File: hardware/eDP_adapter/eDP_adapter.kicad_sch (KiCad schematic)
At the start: 85 parts, among them J1 DF12NB(3.0)-30DS-0.5V(51), J2 DF12NB(3.0)-30DS-0.5V(51), J3 Conn_01x40, J4 Barrel_Jack_MountingPin, Q1 NX3008NBKW,115, U1 NCS8801, U2 TLV62569APDRL, U3 MT3608, U5 TPNCP115ASN120T2G, X1 24MHz, CL=18PF

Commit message: Add I2C connector for touch and replace 40pin touch with 30pin. Separate schematics in sheets. Impedance control on diff pairs
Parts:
- removed C10, C13, C18, C21, C26, C3, C5, C7: 0.1uF, Library:C_0402_1005Metric, symbol Periph-altium-import:0_CAP
- removed C11, C20, C22, C25, C4, C8, C9: 2.2uF, Library:C_0402_1005Metric, symbol Periph-altium-import:0_CAP
- removed C12, C2, C24: 10uF 25V, Capacitor_SMD:C_0805_2012Metric, symbol Periph-altium-import:0_CAP
- removed C6: 100pF, Capacitor_SMD:C_0201_0603Metric, symbol Device:C
- removed D2: 1N5819WS, Diode_SMD:D_SOD-323, symbol Diode:1N5819WS
- removed FB4, FB5, FB6, FB7, FB8, FB9: CBG160808U601T, Inductor_SMD:L_0603_1608Metric, symbol Device:FerriteBead_Small
- removed J1, J2: DF12NB(3.0)-30DS-0.5V(51), Library:DF12NB3030DP05V51, symbol DF12NB_3.0_-30DP-0.5V_51_:DF12NB_3.0_-30DP-0.5V_51_
- removed J3: Conn_01x40, Library:FPC-SMD_40P-P0.50_L4.4-W25.6, symbol Connector_Generic:Conn_01x40
- removed J4: Barrel_Jack_MountingPin, Library:DC-IN-SMD_DC-045A-13A, symbol Connector:Barrel_Jack_Switch_MountingPin
- removed JP1, JP2: SolderJumper_2_Open, Jumper:SolderJumper-2_P1.3mm_Open_RoundedPad1.0x1.5mm, symbol Jumper:SolderJumper_2_Open
- removed JP3: SolderJumper_3_Bridged12, Jumper:SolderJumper-3_P1.3mm_Bridged12_RoundedPad1.0x1.5mm, symbol Jumper:SolderJumper_3_Bridged12
- removed L1: 22uH, Inductor_SMD:L_Cenker_CKCS4020, symbol CKCS201610-2.2UH/M-N_1
- removed L2: 2.2uH, Library:Murata_DFE201612P-2R2M=P2, symbol Periph-altium-import:0_L
- removed Q1: NX3008NBKW,115, Package_TO_SOT_SMD:SOT-323_SC-70, symbol Transistor_FET:2N7002
- removed R10, R13: 0, Resistor_SMD:R_0402_1005Metric, symbol Device:R
- removed R11: 15k, Resistor_SMD:R_0201_0603Metric, symbol Device:R
- removed R12: 4.7k, Resistor_SMD:R_0201_0603Metric, symbol Device:R
- removed R14: 100k, Resistor_SMD:R_0402_1005Metric, symbol Device:R
- removed R15, R19: 10k, Resistor_SMD:R_0402_1005Metric, symbol Device:R
- removed R20: 150K 1%, Resistor_SMD:R_0402_1005Metric, symbol R_0402_EU
- removed R21: 8.06K 1%, Resistor_SMD:R_0402_1005Metric, symbol R_0402_EU_1
- removed R9: 10K, Resistor_SMD:R_0402_1005Metric, symbol Device:R
- removed TP1, TP12, TP13, TP14, TP15, TP16, TP2, TP3, TP4, TP5, TP6, TP7, TP8, TP9: TestPoint_Small, TestPoint:TestPoint_Pad_D1.0mm, symbol Connector:TestPoint_Small
- removed U2: TLV62569APDRL, Package_TO_SOT_SMD:SOT-563, symbol Regulator_Switching:TLV62569DRL
- removed U3: MT3608, Package_TO_SOT_SMD:SOT-23-6, symbol Regulator_Switching:MT3608
- removed U5: TPNCP115ASN120T2G, Package_TO_SOT_SMD:SOT-23-5, symbol Regulator_Linear:NCP115AMX250TCG
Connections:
- net GND: now also C32.1; no longer C32.2
- net XTALI: now also C32.2; no longer C32.1
- net DPO0_P: now reaches C15.1, CR2.2, CR2.9, U1.36 (DPO0_P)
- net DPO1_P: now reaches C23.1, CR2.5, CR2.6, U1.38 (DPO1_P)
- net DPAUX_P: now reaches C17.1, CR1.4, CR1.7, U1.33 (DPAUX_P)
- net DPAUX_N: now reaches C16.1, CR1.5, CR1.6, U1.34 (DPAUX_N)
- net DPO0_N: now reaches C14.1, CR2.1, CR2.10, U1.35 (DPO0_N)
- net DPO1_N: now reaches C1.1, CR2.4, CR2.7, U1.37 (DPO1_N)
- no-connect marks 26 -> 2
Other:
- added sheet IO (eDP_adapter_IO.kicad_sch)
- added sheet POWER (eDP_adapter_power.kicad_sch)
- note removed: "2.5 to 3.3V: HSVDD33 RGB mode (1.8V allowable) or LVDS XVDD33 is for XTAL DVDD33 for digital VIO controls if RGB is down to 1.8V or LVDS 2.5V"
- note removed: "LCD_D0"
- note removed: "LCD_D1"
- note removed: "LCD_D10"
- note removed: "LCD_D11"
- note removed: "LCD_D12"
- note removed: "LCD_D13"
- note removed: "LCD_D14"
- note removed: "LCD_D15"
- note removed: "LCD_D16"
- note removed: "LCD_D17"
- note removed: "LCD_D18"
- note removed: "LCD_D19"
- note removed: "LCD_D2"
- note removed: "LCD_D20"
- note removed: "LCD_D21"
- note removed: "LCD_D22"
- note removed: "LCD_D23"
- note removed: "LCD_D3"
- note removed: "LCD_D4"
- note removed: "LCD_D5"
- note removed: "LCD_D6"
- note removed: "LCD_D7"
- note removed: "LCD_D8"
- note removed: "LCD_D9"
- note removed: "NCS8801 Channel and polarity swap supported Built-in video test pattern Reset defaults (2048x1536) 0x00: default 24-bit / 4 lanes / 1.62Gbps / no hardware training 0x05: no polarity inverse 0x09: normal video 0x0C: RGB mode / NS mode 0x0D: 4-lane order no reverse 0x0F: no LVDS inverse, no ODD/EVEN swap 0x10-0x11: Htotal 2208 (0x08A0) 0x12-0x13: Hstart 10 (0x000A) 0x14-0x15: Hactive 2048 (0x0800) 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"
- note removed: "North connector"
- note removed: "RSTB is active low"
- note removed: "South connector"
- note removed: "TODO: XTAL was MISSING !!! add test points for power (better: solder jumpers to allow disconnection) add 6-pin I2C connector"
- note removed: "TP_RST is active low (GT911 IC) TP_INT is configurable (sets I2C address at startup)"
- note removed: "The IC may require a higher voltage"
- note removed: "Touch panel power: NV156FHM-T01 3.3V B156XTK01.0 5V"
- note removed: "Vth=1.1V"
- note removed: "Vth=1.2V"
- note removed: "Vth=1V"
- note removed: "about 10ms delay (>50us)"
- note removed: "skew < 100mil (LVDS) or 300mil (RGB)"
- note removed: "soldiercrab TLV62569ADRLR"
- moved on the sheet: C1, C14, C15, C16, C17, C19, C23, C32, CR1, CR2, CR3, R1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

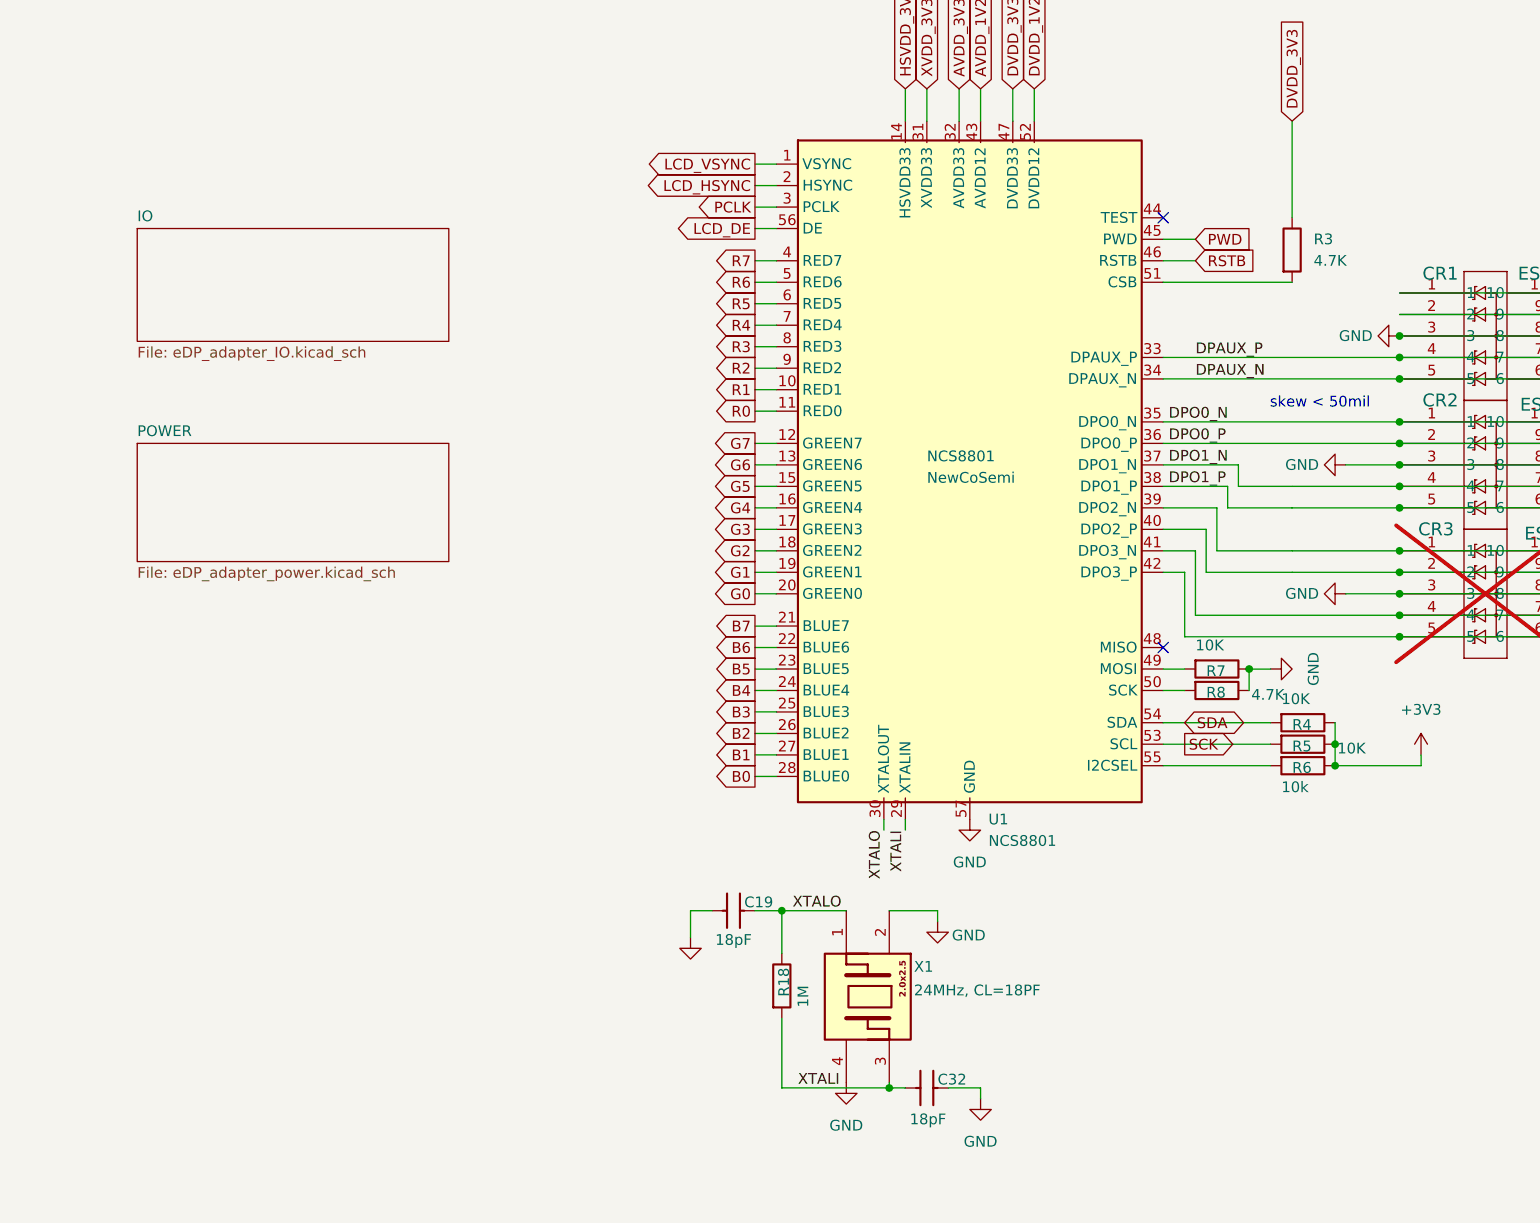
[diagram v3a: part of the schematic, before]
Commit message: change eDP adapter for dual channel LVDS input mode
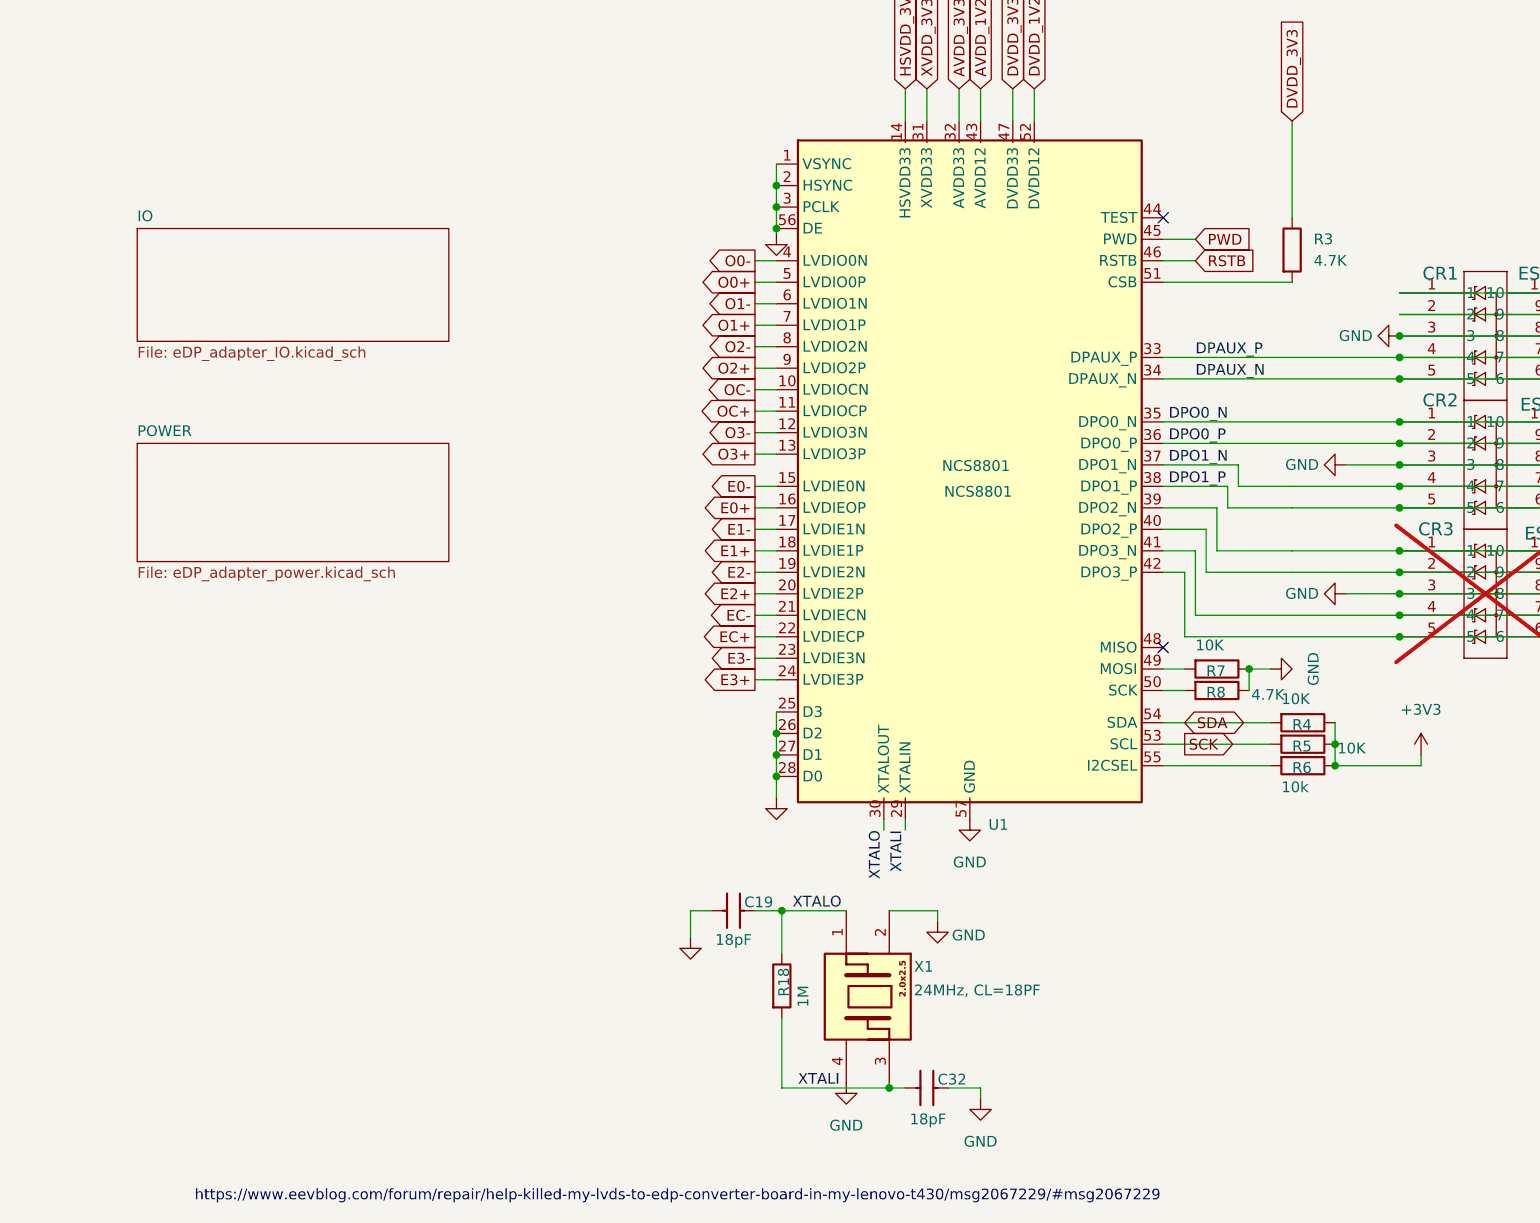
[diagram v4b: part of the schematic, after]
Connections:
- net B0 is gone; now on net GND: U1.28 (D0)
- net B1 is gone; now on net GND: U1.27 (D1)
- net B2 is gone; now on net GND: U1.26 (D2)
- net B3 is gone; now on net GND: U1.25 (D3)
- net LCD_DE is gone; now on net GND: U1.56 (DE)
- net LCD_HSYNC is gone; now on net GND: U1.2 (HSYNC)
- net LCD_VSYNC is gone; now on net GND: U1.1 (VSYNC)
- net PCLK is gone; now on net GND: U1.3 (PCLK)
- net B4 renamed E3+
- net B5 renamed E3-
- net B6 renamed EC+
- net B7 renamed EC-
- net G0 renamed E2+
- net G1 renamed E2-
- net G2 renamed E1+
- net G3 renamed E1-
- net G4 renamed E0+
- net G5 renamed E0-
- net G6 renamed O3+
- net G7 renamed O3-
- net R0 renamed OC+
- net R1 renamed OC-
- net R2 renamed O2+
- net R3 renamed O2-
- net R4 renamed O1+
- net R5 renamed O1-
- net R6 renamed O0+
- net R7 renamed O0-
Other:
- note added: "https://www.eevblog.com/forum/repair/help-killed-my-lvds-to-edp-converter-board-in-my-lenovo-t430/msg2067229/#msg2067229"
- note removed: "skew < 50mil"
